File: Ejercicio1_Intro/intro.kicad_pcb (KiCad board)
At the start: 2 copper layers, 20.3 x 16.5 mm, 5 parts, among them K1 CONN_3

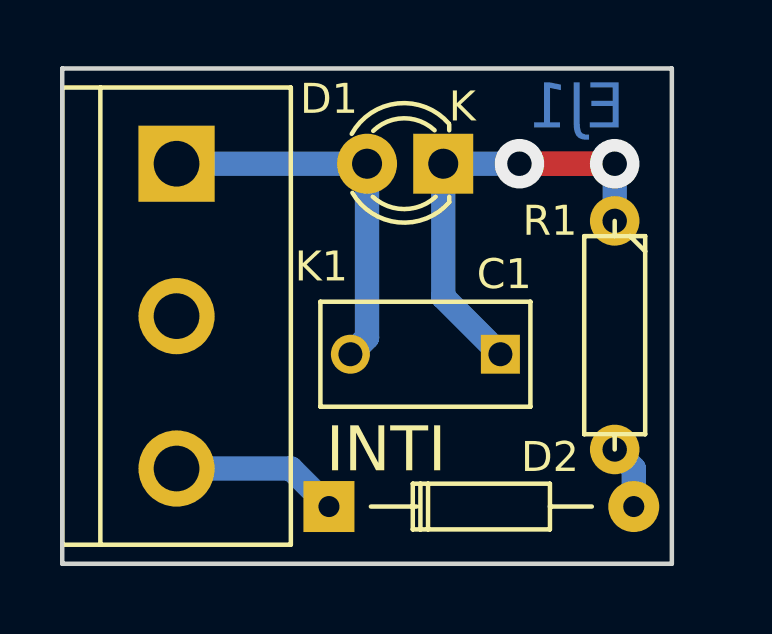
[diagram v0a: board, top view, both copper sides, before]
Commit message: Agregado de la R2.
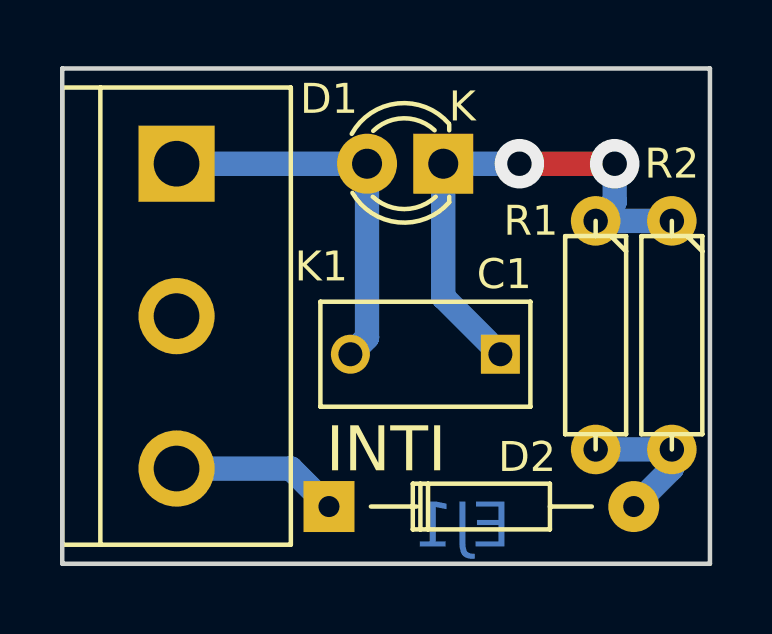
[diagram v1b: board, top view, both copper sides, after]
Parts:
- added R2: 100K, footprints_ej1:R3-LARGE_PADS, F.Cu at (144.8, 96.5)
- moved R1 0.63 mm to (142.2, 96.5)
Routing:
- net Net-(C1-Pad1): track 14.8 -> 17.6 mm
- net Net-(D2-Pad2): track 2.17 -> 4.97 mm
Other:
- board size 20.3 x 16.5 mm -> 21.6 x 16.5 mm
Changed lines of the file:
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@@
 (kicad_pcb (version 4) (host pcbnew "(2015-09-12 BZR 6188)-product")
   (general
-    (links 6)
+    (links 8)
     (no_connects 0)
     (area 124.384999 87.554999 144.855001 104.215001)
     (thickness 1.6)
     (drawings 8)
-    (tracks 14)
+    (tracks 17)
     (zones 0)
-    (modules 5)
+    (modules 6)
     (nets 5)
   )
@@
   )
   (setup
-    (last_trace_width 0.25)
+    (last_trace_width 0.8128)
     (user_trace_width 0.8128)
     (trace_clearance 0.889)
@@
     (descr "Diode, DO-35,  SOD27, Horizontal, RM 10mm")
     (tags "Diode, DO-35, SOD27, Horizontal, RM 10mm, 1N4148,")
-    (fp_text reference D2 (at 7.366 -1.651) (layer F.SilkS)
+    (fp_text reference D2 (at 6.604 -1.651) (layer F.SilkS)
       (effects (font (size 1 1) (thickness 0.15)))
     )
@@
   )
   (module footprints_ej1:R3-LARGE_PADS (layer F.Cu)
-    (at 142.875 96.52 270)
+    (at 142.24 96.52 270)
     (descr "Resitance 3 pas")
     (tags R)
@@
     )
   )
+  (module footprints_ej1:R3-LARGE_PADS (layer F.Cu)
+    (at 144.78 96.52 270)
+    (descr "Resitance 3 pas")
+    (tags R)
+    (fp_text reference R2 (at -5.715 0 360) (layer F.SilkS)
+      (effects (font (size 1 1) (thickness 0.15)))
+    )
+    (fp_text value 100K (at 0 0 270) (layer F.Fab)
+      (effects (font (size 1 1) (thickness 0.15)))
+    )
+    (fp_line (start -3.81 0) (end -3.302 0) (layer F.SilkS) (width 0.15))
+    (fp_line (start 3.81 0) (end 3.302 0) (layer F.SilkS) (width 0.15))
+    (fp_line (start 3.302 0) (end 3.302 -1.016) (layer F.SilkS) (width 0.15))
+    (fp_line (start 3.302 -1.016) (end -3.302 -1.016) (layer F.SilkS) (width 0.15))
+    (fp_line (start -3.302 -1.016) (end -3.302 1.016) (layer F.SilkS) (width 0.15))
+    (fp_line (start -3.302 1.016) (end 3.302 1.016) (layer F.SilkS) (width 0.15))
+    (fp_line (start 3.302 1.016) (end 3.302 0) (layer F.SilkS) (width 0.15))
+    (fp_line (start -3.302 -0.508) (end -2.794 -1.016) (layer F.SilkS) (width 0.15))
+    (pad 1 thru_hole circle (at -3.81 0 270) (size 1.651 1.651) (drill 0.8128) (layers *.Cu *.Mask F.SilkS)
+      (net 1 "Net-(C1-Pad1)"))
+    (pad 2 thru_hole circle (at 3.81 0 270) (size 1.651 1.651) (drill 0.8128) (layers *.Cu *.Mask F.SilkS)
+      (net 3 "Net-(D2-Pad2)"))
+    (model Discret.3dshapes/R3-LARGE_PADS.wrl
+      (at (xyz 0 0 0))
+      (scale (xyz 0.3 0.3 0.3))
+      (rotate (xyz 0 0 0))
+    )
+  )
+  (dimension 21.59 (width 0.3) (layer Dwgs.User)
+    (gr_text 21,590mm (at 135.255 83.105) (layer Dwgs.User)
+      (effects (font (size 1.5 1.5) (thickness 0.3)))
+    )
+    (feature1 (pts (xy 146.05 87.63) (xy 146.05 81.755)))
+    (feature2 (pts (xy 124.46 87.63) (xy 124.46 81.755)))
+    (crossbar (pts (xy 124.46 84.455) (xy 146.05 84.455)))
+    (arrow1a (pts (xy 146.05 84.455) (xy 144.923496 85.041421)))
+    (arrow1b (pts (xy 146.05 84.455) (xy 144.923496 83.868579)))
+    (arrow2a (pts (xy 124.46 84.455) (xy 125.586504 85.041421)))
+    (arrow2b (pts (xy 124.46 84.455) (xy 125.586504 83.868579)))
+  )
+  (dimension 16.51 (width 0.3) (layer Dwgs.User)
+    (gr_text 16,510mm (at 149.305 95.885 270) (layer Dwgs.User)
+      (effects (font (size 1.5 1.5) (thickness 0.3)))
+    )
+    (feature1 (pts (xy 146.05 104.14) (xy 150.655 104.14)))
+    (feature2 (pts (xy 146.05 87.63) (xy 150.655 87.63)))
+    (crossbar (pts (xy 147.955 87.63) (xy 147.955 104.14)))
+    (arrow1a (pts (xy 147.955 104.14) (xy 147.368579 103.013496)))
+    (arrow1b (pts (xy 147.955 104.14) (xy 148.541421 103.013496)))
+    (arrow2a (pts (xy 147.955 87.63) (xy 147.368579 88.756504)))
+    (arrow2b (pts (xy 147.955 87.63) (xy 148.541421 88.756504)))
+  )
+  (gr_line (start 146.05 104.14) (end 124.46 104.14) (angle 90) (layer Edge.Cuts) (width 0.15))
+  (gr_line (start 146.05 87.63) (end 146.05 104.14) (angle 90) (layer Edge.Cuts) (width 0.15))
+  (gr_line (start 124.46 87.63) (end 146.05 87.63) (angle 90) (layer Edge.Cuts) (width 0.15))
   (gr_text INTI (at 135.255 100.33) (layer F.SilkS)
     (effects (font (size 1.5 1.5) (thickness 0.3)))
   )
-  (gr_text EJ1 (at 141.605 88.9) (layer B.Cu)
-    (effects (font (size 1.5 1.5) (thickness 0.3)) (justify mirror))
-  )
-  (dimension 20.32 (width 0.3) (layer Dwgs.User)
-    (gr_text 20,320mm (at 134.62 83.105001) (layer Dwgs.User)
-      (effects (font (size 1.5 1.5) (thickness 0.3)))
-    )
-    (feature1 (pts (xy 124.46 87.63) (xy 124.46 81.755001)))
-    (feature2 (pts (xy 144.78 87.63) (xy 144.78 81.755001)))
-    (crossbar (pts (xy 144.78 84.455001) (xy 124.46 84.455001)))
-    (arrow1a (pts (xy 124.46 84.455001) (xy 125.586504 83.86858)))
-    (arrow1b (pts (xy 124.46 84.455001) (xy 125.586504 85.041422)))
-    (arrow2a (pts (xy 144.78 84.455001) (xy 143.653496 83.86858)))
-    (arrow2b (pts (xy 144.78 84.455001) (xy 143.653496 85.041422)))
-  )
-  (dimension 16.51 (width 0.3) (layer Dwgs.User)
-    (gr_text 16,510mm (at 148.67 95.885 270) (layer Dwgs.User)
-      (effects (font (size 1.5 1.5) (thickness 0.3)))
-    )
-    (feature1 (pts (xy 144.78 104.14) (xy 150.02 104.14)))
-    (feature2 (pts (xy 144.78 87.63) (xy 150.02 87.63)))
-    (crossbar (pts (xy 147.32 87.63) (xy 147.32 104.14)))
-    (arrow1a (pts (xy 147.32 104.14) (xy 146.733579 103.013496)))
-    (arrow1b (pts (xy 147.32 104.14) (xy 147.906421 103.013496)))
-    (arrow2a (pts (xy 147.32 87.63) (xy 146.733579 88.756504)))
-    (arrow2b (pts (xy 147.32 87.63) (xy 147.906421 88.756504)))
+  (gr_text EJ1 (at 137.795 102.87) (layer B.Cu)
+    (effects (font (size 1.5 1.5) (thickness 0.25)) (justify mirror))
   )
   (gr_line (start 124.46 104.14) (end 124.46 87.63) (angle 90) (layer Edge.Cuts) (width 0.15))
-  (gr_line (start 144.78 104.14) (end 124.46 104.14) (angle 90) (layer Edge.Cuts) (width 0.15))
-  (gr_line (start 144.78 87.63) (end 144.78 104.14) (angle 90) (layer Edge.Cuts) (width 0.15))
-  (gr_line (start 124.46 87.63) (end 144.78 87.63) (angle 90) (layer Edge.Cuts) (width 0.15))
+  (segment (start 142.24 92.71) (end 144.78 92.71) (width 0.8128) (layer B.Cu) (net 1))
+  (segment (start 142.875 90.805) (end 142.875 92.075) (width 0.8128) (layer B.Cu) (net 1))
+  (via (at 139.7 90.805) (size 1.651) (drill 0.8128) (layers F.Cu B.Cu) (net 1))
+  (segment (start 139.7 90.805) (end 142.875 90.805) (width 0.8128) (layer F.Cu) (net 1))
+  (via (at 142.875 90.805) (size 1.651) (drill 0.8128) (layers F.Cu B.Cu) (net 1))
   (segment (start 137.16 90.805) (end 139.7 90.805) (width 0.8128) (layer B.Cu) (net 1))
-  (segment (start 142.875 90.805) (end 142.875 92.71) (width 0.8128) (layer B.Cu) (net 1))
-  (via (at 142.875 90.805) (size 1.651) (drill 0.8128) (layers F.Cu B.Cu) (net 1))
-  (segment (start 139.7 90.805) (end 142.875 90.805) (width 0.8128) (layer F.Cu) (net 1))
-  (via (at 139.7 90.805) (size 1.651) (drill 0.8128) (layers F.Cu B.Cu) (net 1))
+  (segment (start 142.875 92.075) (end 142.24 92.71) (width 0.8128) (layer B.Cu) (net 1))
   (segment (start 137.16 90.805) (end 137.16 95.25) (width 0.8128) (layer B.Cu) (net 1))
   (segment (start 137.16 95.25) (end 139.065 97.155) (width 0.8128) (layer B.Cu) (net 1))
@@
   (segment (start 134.62 96.6) (end 134.065 97.155) (width 0.8128) (layer B.Cu) (net 2))
   (segment (start 128.27 90.805) (end 134.62 90.805) (width 0.8128) (layer B.Cu) (net 2))
-  (segment (start 142.875 100.33) (end 143.51052 100.96552) (width 0.8128) (layer B.Cu) (net 3))
-  (segment (start 143.51052 100.96552) (end 143.51052 102.23246) (width 0.8128) (layer B.Cu) (net 3))
+  (segment (start 144.78 100.33) (end 144.78 100.96298) (width 0.8128) (layer B.Cu) (net 3))
+  (segment (start 144.78 100.96298) (end 143.51052 102.23246) (width 0.8128) (layer B.Cu) (net 3))
+  (segment (start 142.24 100.33) (end 144.78 100.33) (width 0.8128) (layer B.Cu) (net 3))
   (segment (start 133.35052 102.23246) (end 132.08306 100.965) (width 0.8128) (layer B.Cu) (net 4))
   (segment (start 132.08306 100.965) (end 128.27 100.965) (width 0.8128) (layer B.Cu) (net 4))
